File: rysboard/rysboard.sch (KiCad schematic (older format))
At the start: 9 parts, among them J1 RPi4, J17 Conn_01x03, J18 Conn_01x05, U4 STM32G031K8Ux

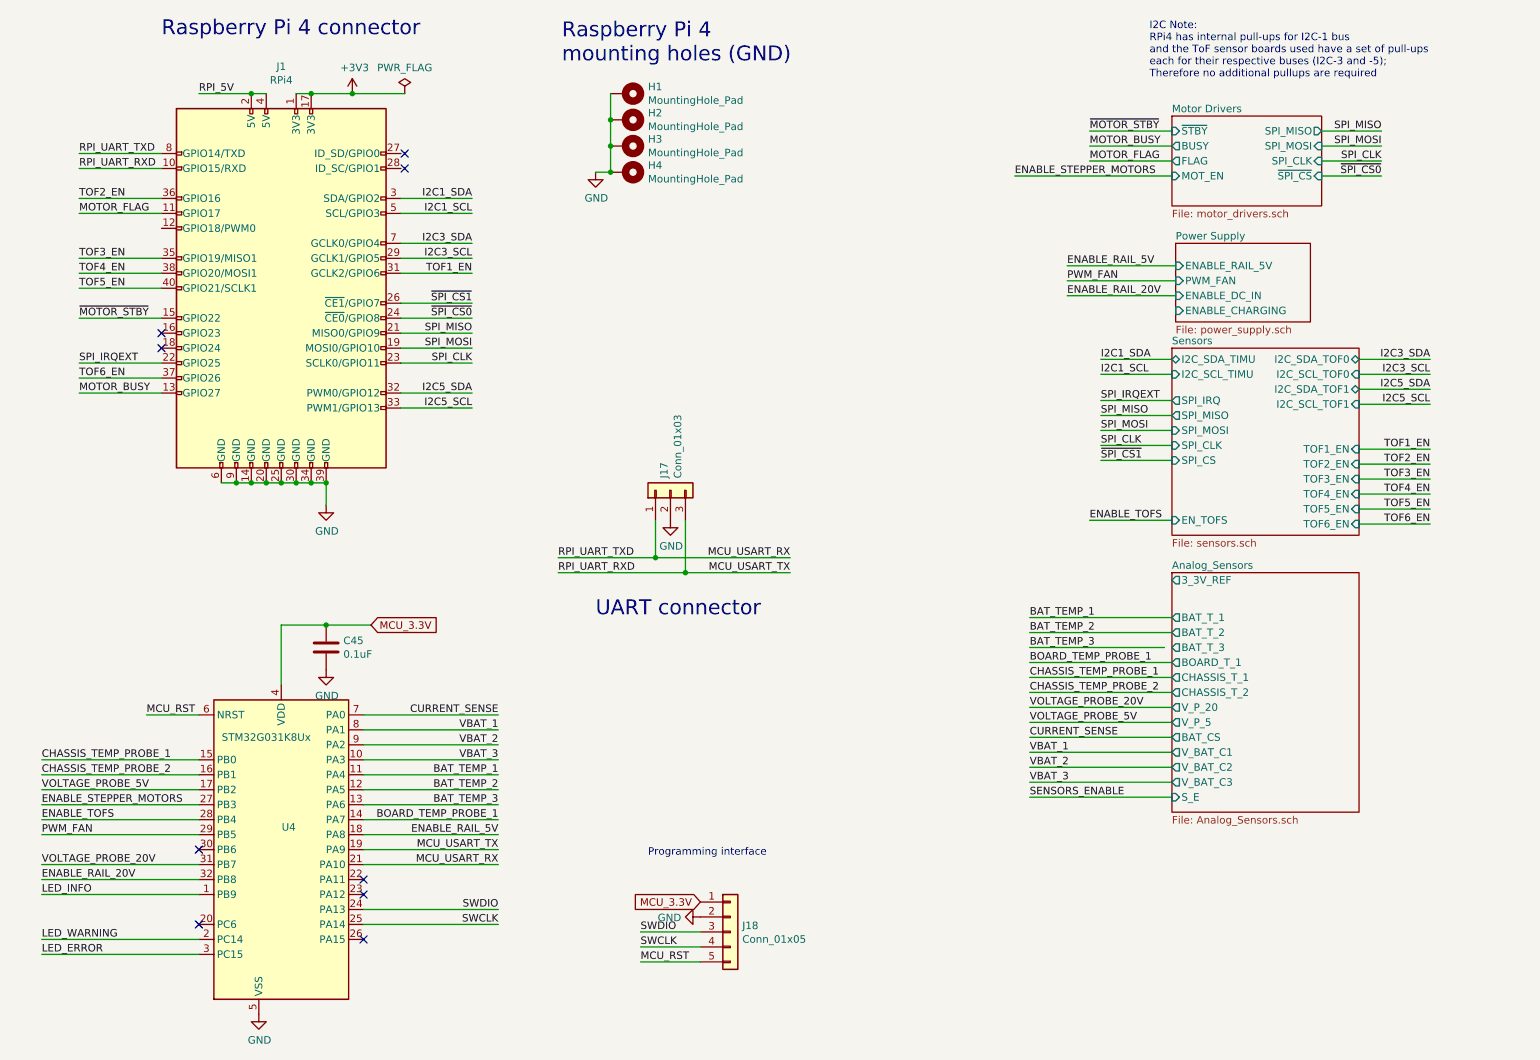
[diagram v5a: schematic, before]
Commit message: LTC4007 done
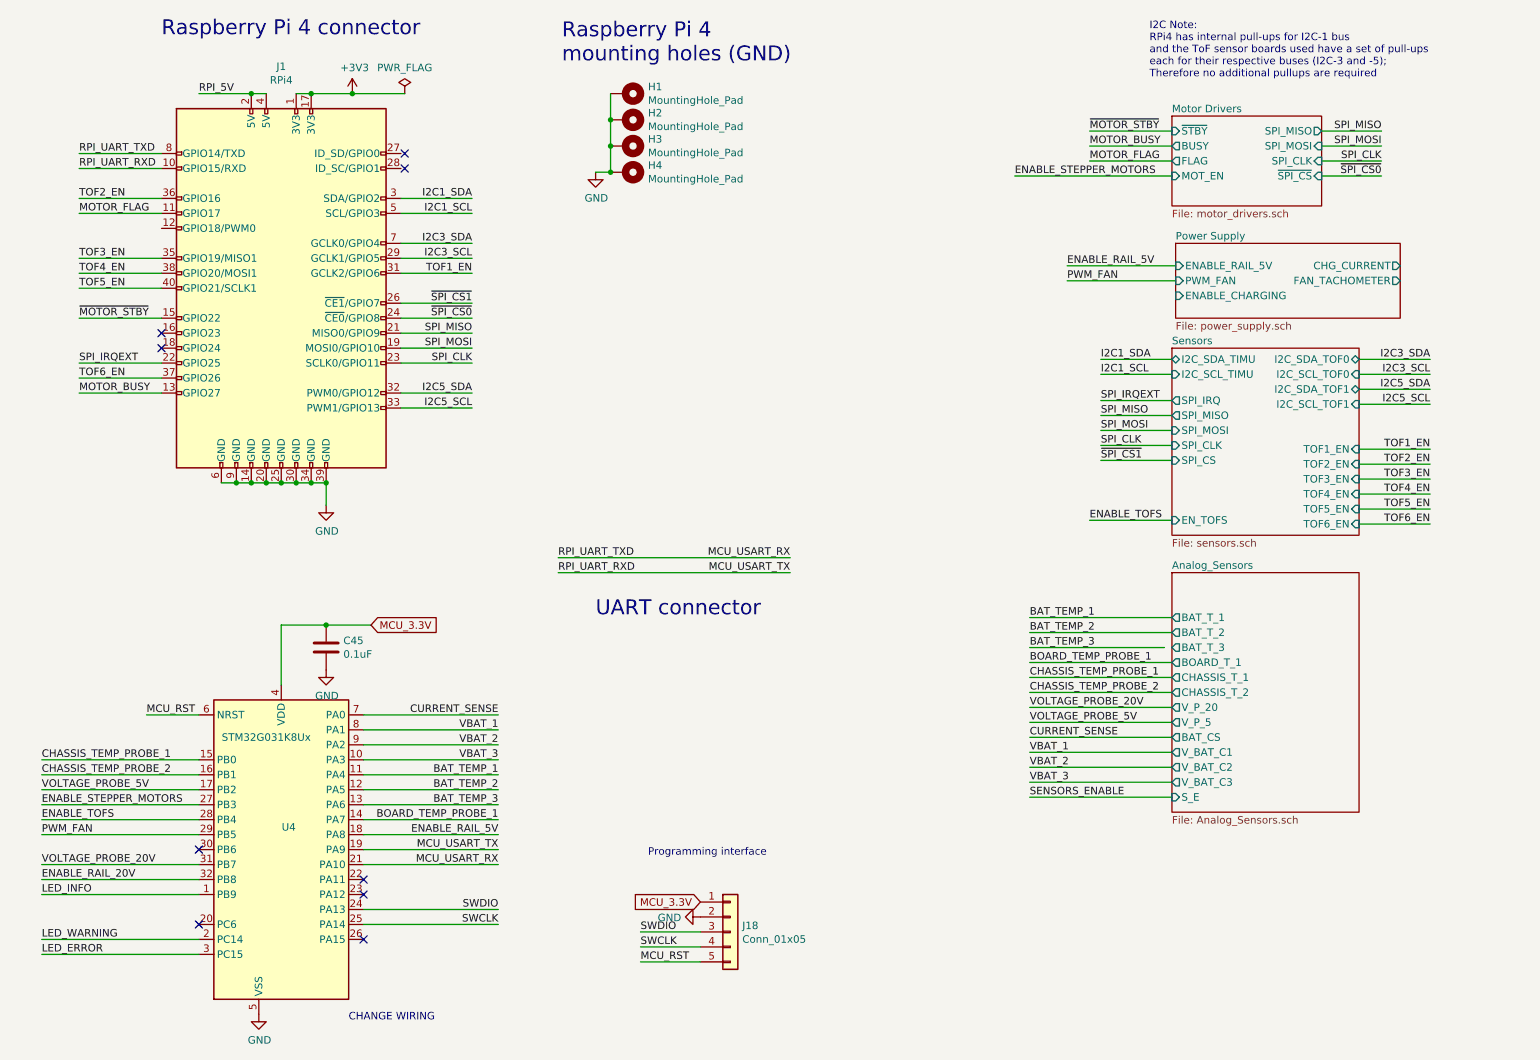
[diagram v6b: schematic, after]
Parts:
- removed J17: Conn_01x03, Connector_PinHeader_2.54mm:PinHeader_1x03_P2.54mm_Vertical, symbol Connector_Generic:Conn_01x03
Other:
- note added: "CHANGE WIRING\n"
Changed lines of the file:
@@
 Raspberry Pi 4 connector
 $Sheet
-S 8275 2200 900  525
+S 8275 2200 1500 500
 U 5E8FCBC6
 F0 "Power Supply" 50
@@
 F2 "ENABLE_RAIL_5V" I L 8275 2350 50
 F3 "PWM_FAN" I L 8275 2450 50
-F4 "ENABLE_DC_IN" I L 8275 2550 50
-F5 "ENABLE_CHARGING" I L 8275 2650 50
+F4 "ENABLE_CHARGING" I L 8275 2550 50
+F5 "CHG_CURRENT" O R 9775 2350 50
+F6 "FAN_TACHOMETER" O R 9775 2450 50
 $EndSheet
 Text Label 3575 2700 2    50   ~ 0
@@
 F19 "EN_TOFS" I L 8250 4050 50
 $EndSheet
-$Comp
-L Connector_Generic:Conn_01x03 J17
-U 1 1 5EA0F66D
-P 4900 3850
-F 0 "J17" H 4980 3892 50  0000 L CNN
-F 1 "Conn_01x03" H 4980 3801 50  0000 L CNN
-F 2 "Connector_PinHeader_2.54mm:PinHeader_1x03_P2.54mm_Vertical" H 4900 3850 50  0001 C CNN
-F 3 "~" H 4900 3850 50  0001 C CNN
-	1    4900 3850
-	0    -1   -1   0
-$EndComp
 Text Label 4150 4300 0    50   ~ 0
 RPI_UART_TXD
@@
 Wire Wire Line
 	950  1600 1500 1600
-$Comp
-L power:GND #PWR017
-U 1 1 6046B140
-P 4900 4050
-F 0 "#PWR017" H 4900 3800 50  0001 C CNN
-F 1 "GND" H 4905 3877 50  0000 C CNN
-F 2 "" H 4900 4050 50  0001 C CNN
-F 3 "" H 4900 4050 50  0001 C CNN
-	1    4900 4050
-	1    0    0    -1
-$EndComp
 Text Label 5700 4300 2    50   ~ 0
 MCU_USART_RX
 Text Label 5700 4400 2    50   ~ 0
 MCU_USART_TX
-Wire Wire Line
-	4800 4300 4800 4050
-Wire Wire Line
-	5000 4400 5000 4050
-Wire Wire Line
-	4800 4300 5700 4300
-Wire Wire Line
-	5000 4400 5700 4400
-Wire Wire Line
-	4150 4300 4800 4300
-Connection ~ 4800 4300
-Wire Wire Line
-	4150 4400 5000 4400
-Connection ~ 5000 4400
 Text Label 7550 2350 0    50   ~ 0
 ENABLE_RAIL_5V
 Text Label 7550 2450 0    50   ~ 0
 PWM_FAN
-Text Label 7550 2550 0    50   ~ 0
-ENABLE_RAIL_20V
 Wire Wire Line
 	7550 2350 8275 2350
 Wire Wire Line
 	7550 2450 8275 2450
-Wire Wire Line
-	7550 2550 8275 2550
 Text Label 7700 4050 0    50   ~ 0
 ENABLE_TOFS
@@
 F13 "V_BAT_C3" O L 8250 5800 50
 F14 "S_E" I L 8250 5900 50
-F15 "3_3V_REF" O L 8250 4450 50
 $EndSheet
 Text Label 7300 5100 0    50   ~ 0
@@
 Text Label 700  5750 0    50   ~ 0
 CHASSIS_TEMP_PROBE_2
+Wire Wire Line
+	4150 4300 5700 4300
+Wire Wire Line
+	4150 4400 5700 4400
+Text Notes 2750 7400 0    50   ~ 0
+CHANGE WIRING\n
 $EndSCHEMATC

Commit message: Even More footprints
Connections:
- net BOARD_TEMP_PROBE_1: now also U4.17 (PB2); no longer U4.14 (PA7)
- net CHASSIS_TEMP_PROBE_1: now also U4.9 (PA2); no longer U4.15 (PB0)
- net CHASSIS_TEMP_PROBE_2: now also U4.10 (PA3); no longer U4.16 (PB1)
- net CURRENT_SENSE: no longer U4.7 (PA0)
- net ENABLE_RAIL_5V: now also U4.20 (PC6); no longer U4.18 (PA8)
- net VBAT_1: now also U4.14 (PA7); no longer U4.8 (PA1)
- net VBAT_2: now also U4.15 (PB0); no longer U4.9 (PA2)
- net VBAT_3: now also U4.16 (PB1); no longer U4.10 (PA3)
- net VOLTAGE_PROBE_5V: now also U4.8 (PA1); no longer U4.17 (PB2)
- net BAT_CURRENT: now reaches U4.22 (PA11)
- net CHG_CURRENT: now reaches U4.23 (PA12)
- net FAN_TACH: now reaches U4.30 (PB6)
- net ENABLE_RAIL_20V renamed ENABLE_CHARGING
- net LED_ERROR renamed LED_B
- net LED_INFO renamed LED_R
- net LED_WARNING renamed LED_G
- new net ENABLE_SENSORS: U4.18 (PA8)
- no-connect marks 9 -> 6
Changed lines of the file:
@@
 	2600 3950 2600 3800
 Connection ~ 2600 3800
-Text Label 3750 6750 2    50   ~ 0
+Text Label 3825 6750 2    50   ~ 0
 SWCLK
-Text Label 3750 6650 2    50   ~ 0
+Text Label 3825 6650 2    50   ~ 0
 SWDIO
 Text Label 1400 5350 0    50   ~ 0
@@
 	1400 5350 1750 5350
 Text Label 700  6550 0    50   ~ 0
-LED_INFO
+LED_R
 Text Label 700  6850 0    50   ~ 0
-LED_WARNING
+LED_G
 Text Label 700  6950 0    50   ~ 0
-LED_ERROR
-Text Label 3750 5350 2    50   ~ 0
-CURRENT_SENSE
-Text Label 3750 5450 2    50   ~ 0
+LED_B
+Text Label 3825 6450 2    50   ~ 0
+BAT_CURRENT
+Text Label 3825 6050 2    50   ~ 0
 VBAT_1
-Text Label 3750 5550 2    50   ~ 0
+Text Label 700  5650 0    50   ~ 0
 VBAT_2
-Text Label 3750 5650 2    50   ~ 0
+Text Label 700  5750 0    50   ~ 0
 VBAT_3
-Text Label 3750 5750 2    50   ~ 0
+Text Label 3825 5750 2    50   ~ 0
 BAT_TEMP_1
-Text Label 3750 5850 2    50   ~ 0
+Text Label 3825 5850 2    50   ~ 0
 BAT_TEMP_2
-Text Label 3750 5950 2    50   ~ 0
+Text Label 3825 5950 2    50   ~ 0
 BAT_TEMP_3
-Text Label 3750 6050 2    50   ~ 0
+Text Label 700  5850 0    50   ~ 0
 BOARD_TEMP_PROBE_1
-Text Label 700  5850 0    50   ~ 0
+Text Label 3825 5450 2    50   ~ 0
 VOLTAGE_PROBE_5V
-Text Label 3750 6150 2    50   ~ 0
+Text Label 700  6750 0    50   ~ 0
 ENABLE_RAIL_5V
-Text Label 3750 6250 2    50   ~ 0
+Text Label 3825 6250 2    50   ~ 0
 MCU_USART_TX
-Text Label 3750 6350 2    50   ~ 0
+Text Label 3825 6350 2    50   ~ 0
 MCU_USART_RX
 Text Label 700  5950 0    50   ~ 0
@@
 VOLTAGE_PROBE_20V
 Text Label 700  6450 0    50   ~ 0
-ENABLE_RAIL_20V
-Wire Wire Line
-	2850 6750 3750 6750
-Wire Wire Line
-	2850 6650 3750 6650
-Wire Wire Line
-	3750 6350 2850 6350
-Wire Wire Line
-	3750 6250 2850 6250
-Wire Wire Line
-	3750 6150 2850 6150
-Wire Wire Line
-	2850 6050 3750 6050
-Wire Wire Line
-	3750 5950 2850 5950
-Wire Wire Line
-	2850 5850 3750 5850
-Wire Wire Line
-	3750 5750 2850 5750
-Wire Wire Line
-	2850 5650 3750 5650
-Wire Wire Line
-	3750 5550 2850 5550
-Wire Wire Line
-	2850 5450 3750 5450
-Wire Wire Line
-	2850 5350 3750 5350
+ENABLE_CHARGING
 Wire Wire Line
 	700  6950 1750 6950
@@
 $EndComp
 NoConn ~ 2850 6850
-NoConn ~ 2850 6550
-NoConn ~ 2850 6450
-NoConn ~ 1750 6750
-NoConn ~ 1750 6250
 Text Label 7200 1750 0    50   ~ 0
 ENABLE_STEPPER_MOTORS
@@
 	9650 1750 9250 1750
 Text Label 7300 5900 0    50   ~ 0
-SENSORS_ENABLE
+ENABLE_SENSORS
 Wire Wire Line
 	7300 5900 8250 5900
@@
 	1    0    0    -1
 $EndComp
-Text Label 700  5650 0    50   ~ 0
+Text Label 3825 5550 2    50   ~ 0
 CHASSIS_TEMP_PROBE_1
-Text Label 700  5750 0    50   ~ 0
+Text Label 3825 5650 2    50   ~ 0
 CHASSIS_TEMP_PROBE_2
 Wire Wire Line
@@
 Text Notes 2750 7400 0    50   ~ 0
 CHANGE WIRING\n
+Text Label 7550 2550 0    50   ~ 0
+ENABLE_CHARGING
+Wire Wire Line
+	7550 2550 8275 2550
+Text Label 10375 2450 2    50   ~ 0
+FAN_TACH
+Text Label 10375 2350 2    50   ~ 0
+CHG_CURRENT
+Wire Wire Line
+	9775 2450 10375 2450
+Wire Wire Line
+	9775 2350 10375 2350
+Text Label 3825 6550 2    50   ~ 0
+CHG_CURRENT
+Wire Wire Line
+	2850 5550 3825 5550
+Wire Wire Line
+	2850 5650 3825 5650
+Wire Wire Line
+	2850 6050 3825 6050
+Wire Wire Line
+	2850 5950 3825 5950
+Wire Wire Line
+	2850 5850 3825 5850
+Wire Wire Line
+	2850 5750 3825 5750
+Wire Wire Line
+	2850 5450 3825 5450
+Wire Wire Line
+	2850 6150 3825 6150
+Wire Wire Line
+	2850 6750 3825 6750
+Wire Wire Line
+	2850 6650 3825 6650
+Wire Wire Line
+	2850 6550 3825 6550
+Wire Wire Line
+	2850 6450 3825 6450
+Wire Wire Line
+	2850 6350 3825 6350
+Wire Wire Line
+	2850 6250 3825 6250
+Text Label 700  6250 0    50   ~ 0
+FAN_TACH
+Wire Wire Line
+	1750 6250 700  6250
+Wire Wire Line
+	700  6750 1750 6750
+NoConn ~ 3825 5350
+Wire Wire Line
+	2850 5350 3825 5350
+Text Label 3825 6150 2    50   ~ 0
+ENABLE_SENSORS
 $EndSCHEMATC

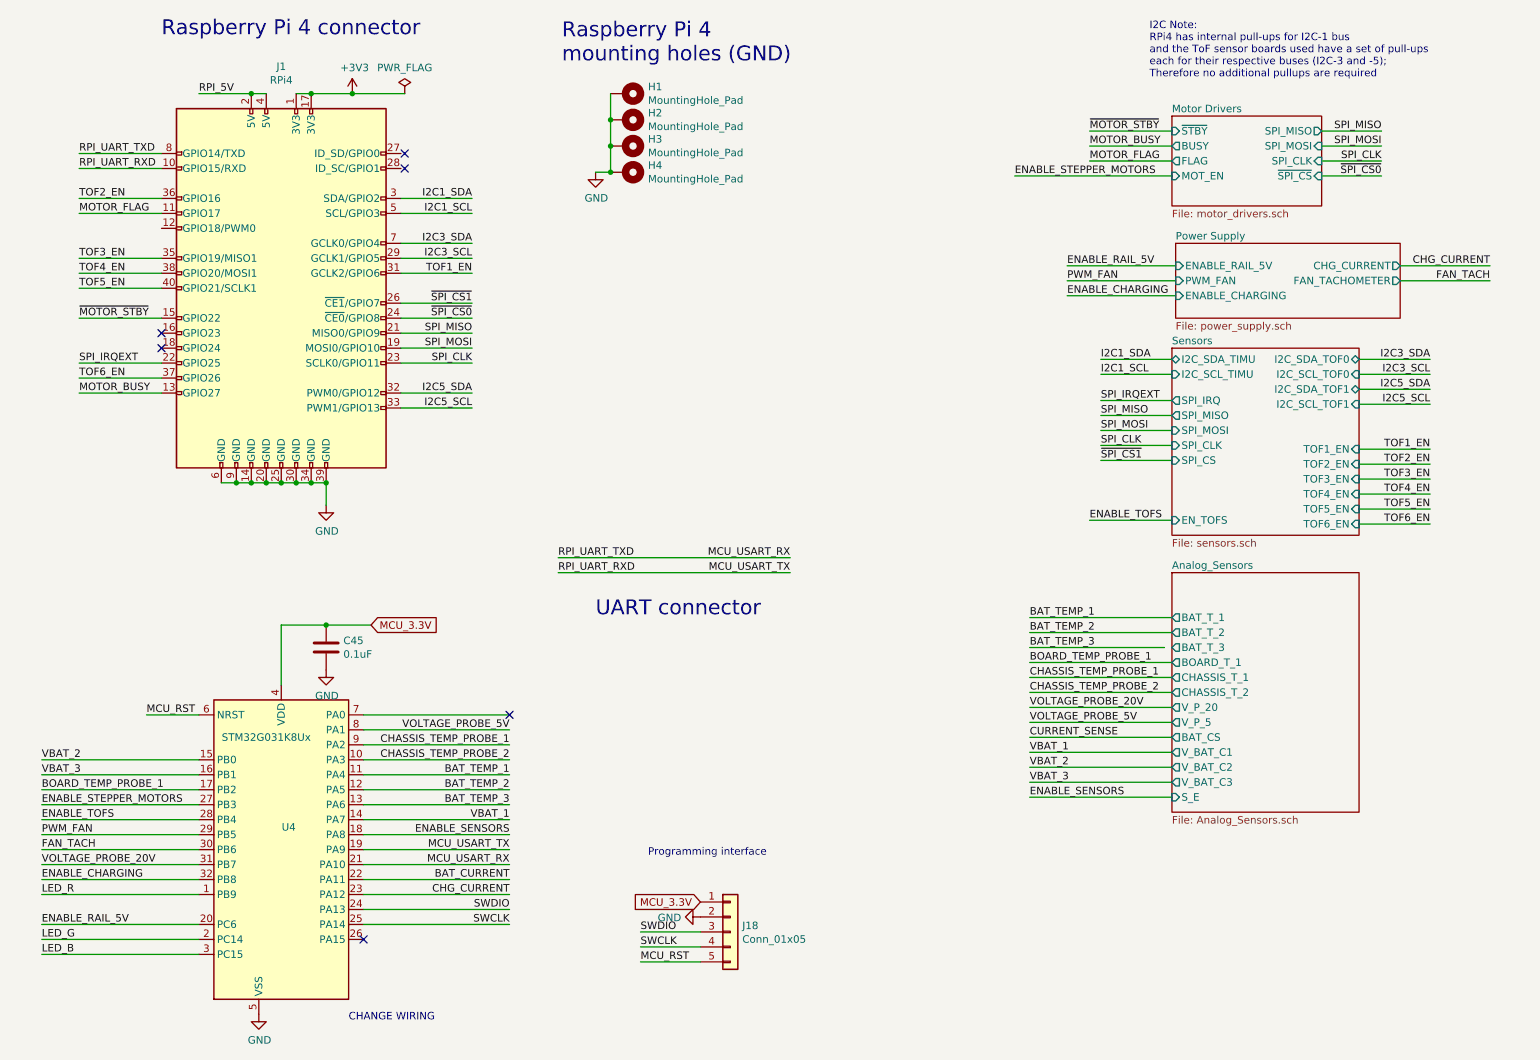
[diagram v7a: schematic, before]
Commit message: More Work. RPI can now programm STM32 via GPIO
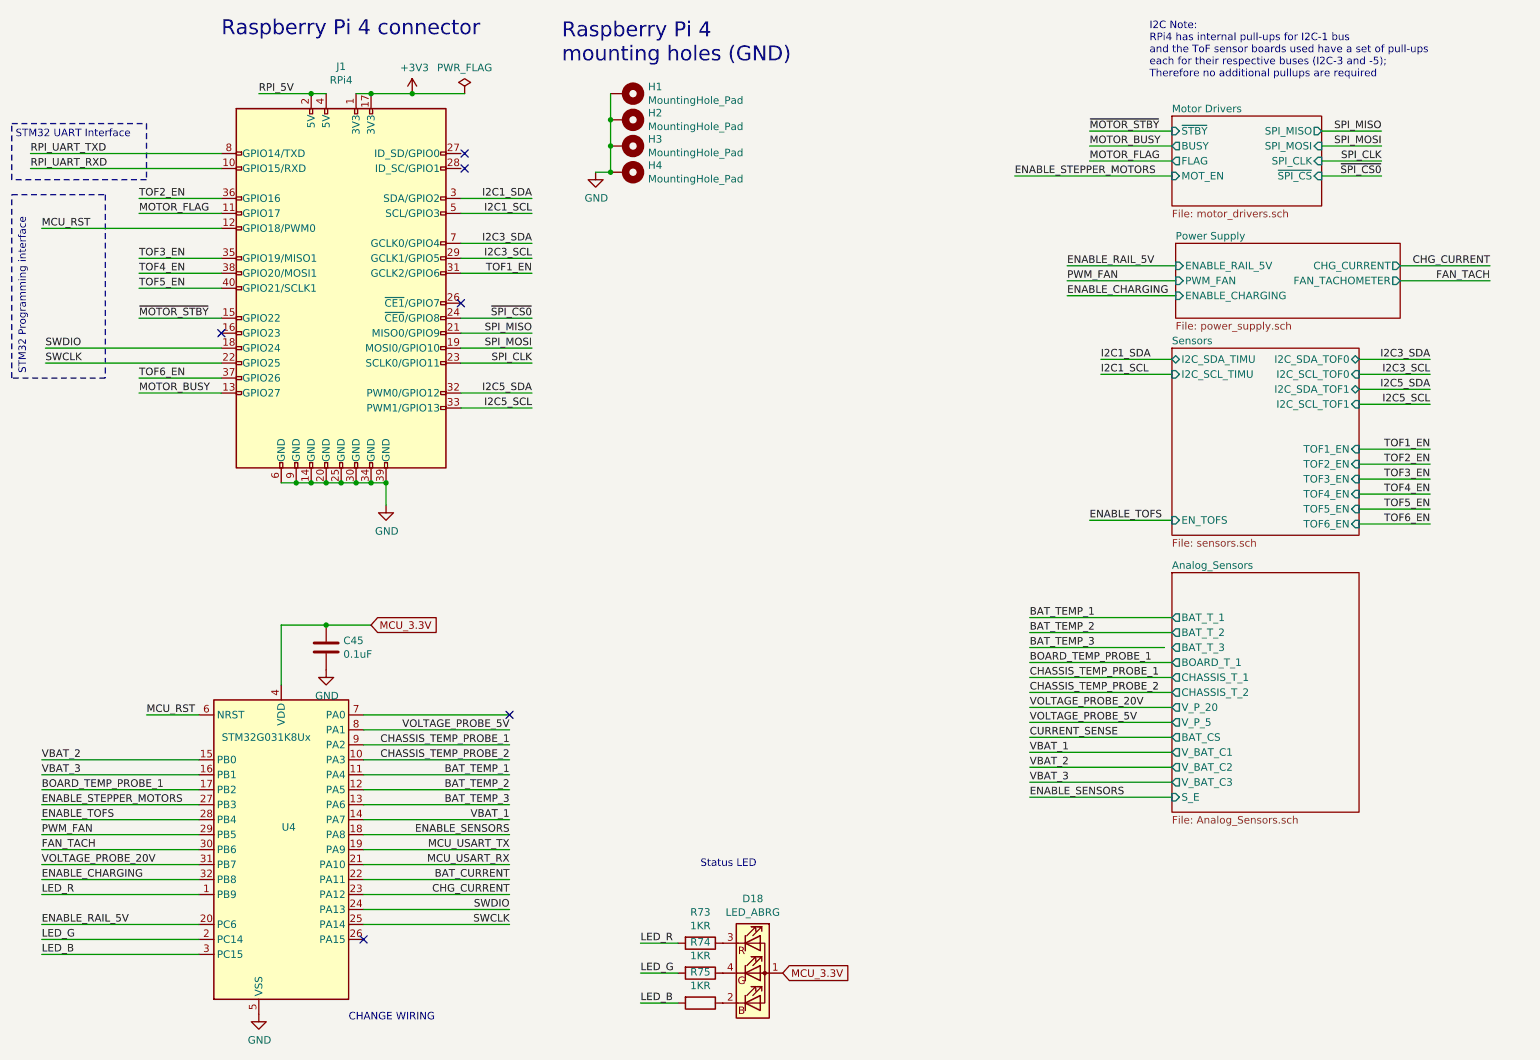
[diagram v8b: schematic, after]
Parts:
- removed J18: Conn_01x05, Connector_PinHeader_1.00mm:PinHeader_1x05_P1.00mm_Vertical, symbol Connector_Generic:Conn_01x05
- added D18: LED_ABRG, rysboard:KRTBDWLM32.32-T4U6-JW+AAAB-J3+R4S6-5V, symbol Device:LED_ABRG
- added R73, R74, R75: 1KR, Resistor_SMD:R_0603_1608Metric, symbol Device:R
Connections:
- net SPI_IRQEXT is gone; now on net SWCLK: J1.22 (GPIO25)
- net LED_B: now also R75.2
- net LED_G: now also R74.2
- net LED_R: now also R73.2
- net MCU_3.3V: now also D18.1 (A)
- net MCU_RST: now also J1.12 (GPIO18/PWM0)
- net MCU_USART_RX: no longer J1.8 (GPIO14/TXD)
- net MCU_USART_TX: no longer J1.10 (GPIO15/RXD)
- net SWDIO: now also J1.18 (GPIO24)
- net ~SPI_CS1: no longer names the net of J1.26 (~CE1~/GPIO7)
- new net: D18.2 (BK), R75.1
- new net: D18.3 (RK), R73.1
- new net: D18.4 (GK), R74.1
- new net RPI_UART_RXD: J1.10 (GPIO15/RXD)
- new net RPI_UART_TXD: J1.8 (GPIO14/TXD)
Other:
- note added: "STM32 Programming interface\n"
- note added: "STM32 UART Interface\n"
- note added: "Status LED"
- note removed: "Programming interface\n"
- note removed: "UART connector"
- moved on the sheet: J1
